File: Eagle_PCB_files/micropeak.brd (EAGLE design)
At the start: 100 x 80 mm, 15 parts, among them U1 ATTINY85-20MUR, U2 MS5611-01BA03

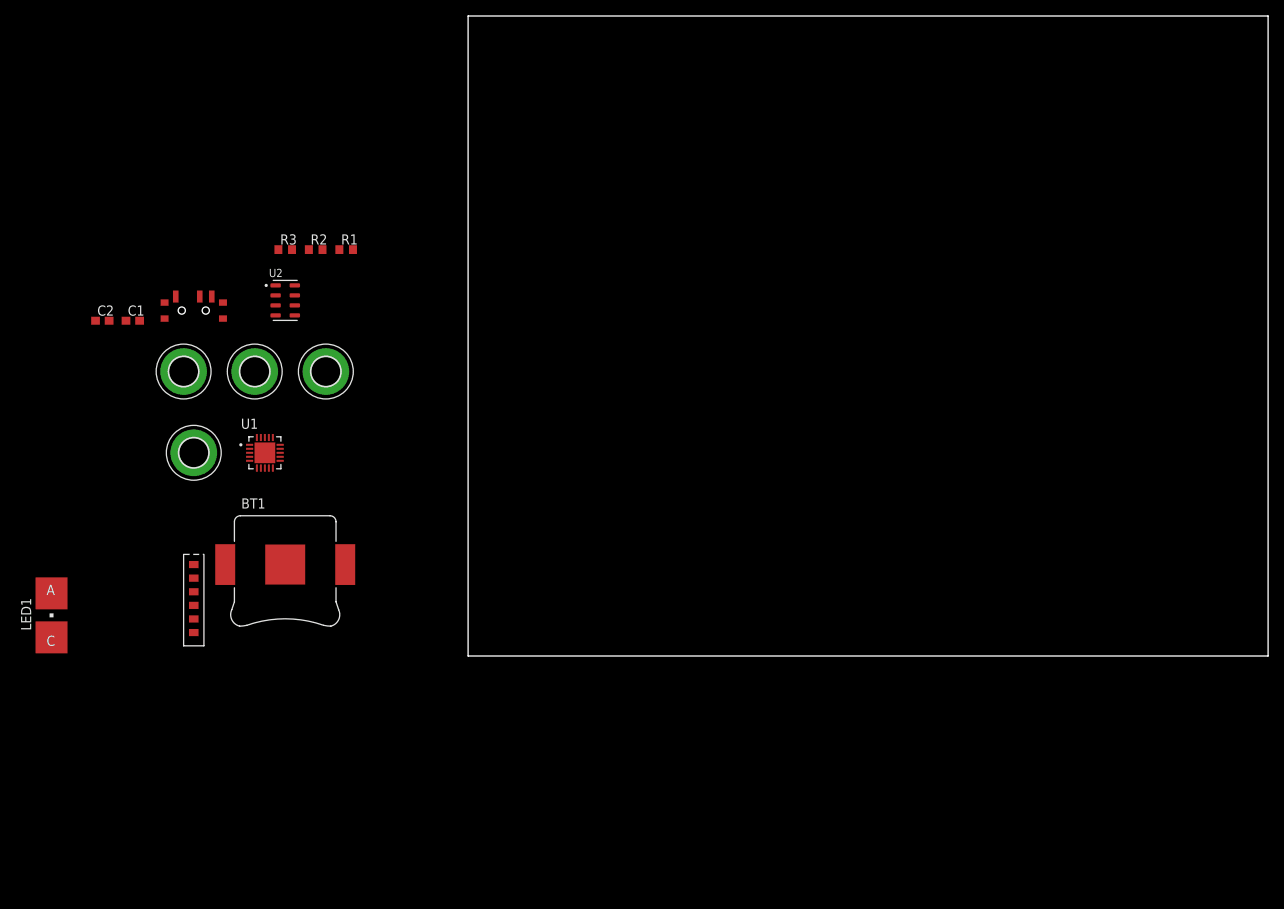
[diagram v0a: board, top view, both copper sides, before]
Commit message: replaced mounting holes with correct size hole
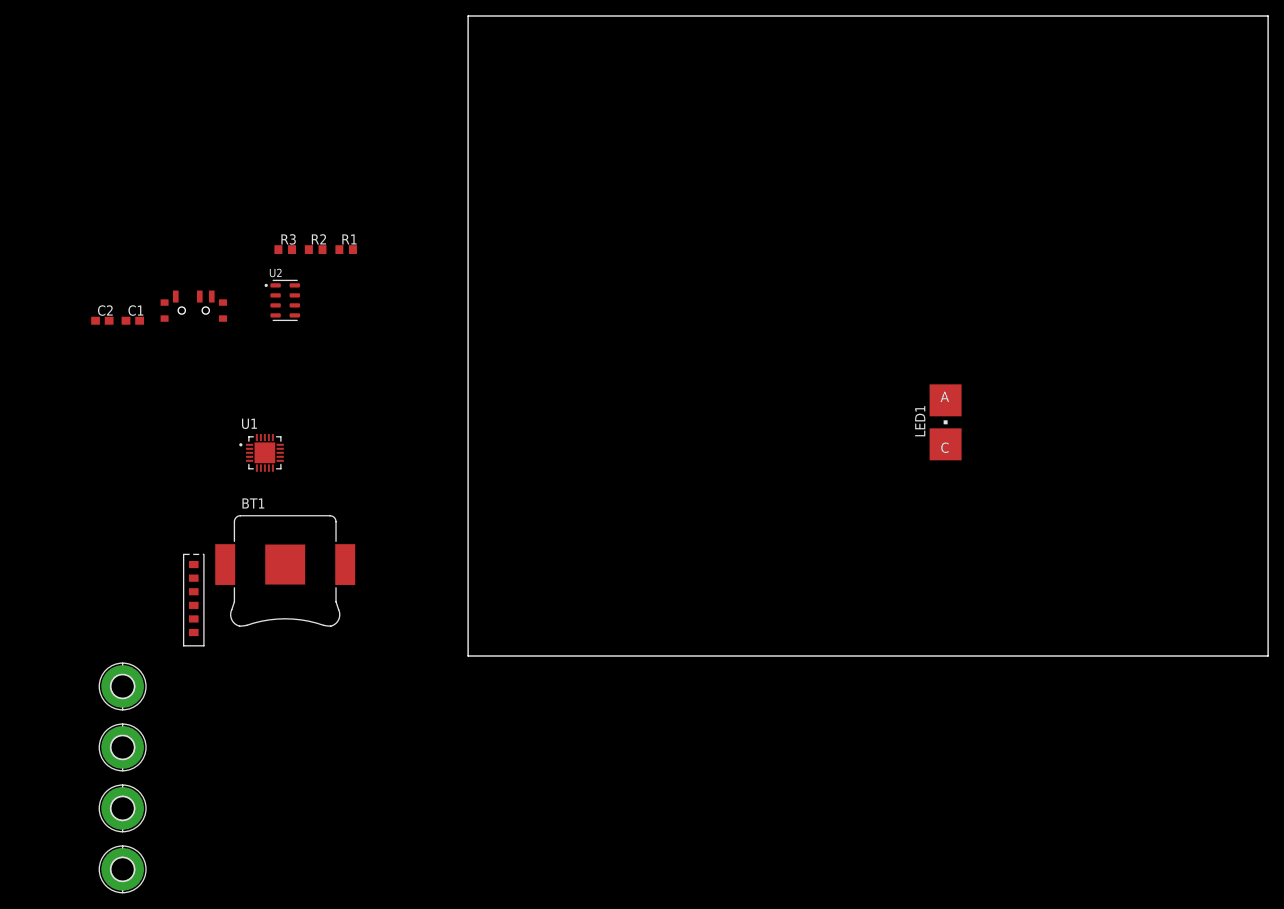
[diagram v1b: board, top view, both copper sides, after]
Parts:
- removed H5: MOUNT-PAD-ROUND3.6, holes:3,6-PAD
- added H4: MOUNT-PAD-ROUND2.8, holes:2,8-PAD
- H1, H2, H3: value MOUNT-PAD-ROUND3.6 -> MOUNT-PAD-ROUND2.8; device holes:3,6-PAD -> holes:2,8-PAD
- moved LED1 114.3 mm to (59.7, 29.2)
- moved H3 64.4 mm to (-43.2, -26.7)
- moved H2 60.2 mm to (-43.2, -19.1)
- moved H1 37.9 mm to (-43.2, -11.4)
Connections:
- net +3V3: now also H1.B2,8, H2.B2,8, H3.B2,8, H4.B2,8; no longer H1.B3,6, H2.B3,6, H3.B3,6, H5.B3,6
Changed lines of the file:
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@@
 <attribute name="VALUE" x="-46.355" y="40.005" size="1.27" layer="27"/>
-</element>
-<element name="H1" library="holes" library_urn="urn:adsk.eagle:library:237" package="3,6-PAD" package3d_urn="urn:adsk.eagle:package:14284/1" value="MOUNT-PAD-ROUND3.6" x="-34.29" y="25.4" smashed="yes">
-<attribute name="POPULARITY" value="0" x="0" y="0" size="1.778" layer="27" display="off"/>
-</element>
-<element name="H2" library="holes" library_urn="urn:adsk.eagle:library:237" package="3,6-PAD" package3d_urn="urn:adsk.eagle:package:14284/1" value="MOUNT-PAD-ROUND3.6" x="-17.78" y="35.56" smashed="yes">
-<attribute name="POPULARITY" value="0" x="0" y="0" size="1.778" layer="27" display="off"/>
-</element>
-<element name="H3" library="holes" library_urn="urn:adsk.eagle:library:237" package="3,6-PAD" package3d_urn="urn:adsk.eagle:package:14284/1" value="MOUNT-PAD-ROUND3.6" x="-26.67" y="35.56" smashed="yes">
-<attribute name="POPULARITY" value="0" x="0" y="0" size="1.778" layer="27" display="off"/>
-</element>
-<element name="H5" library="holes" library_urn="urn:adsk.eagle:library:237" package="3,6-PAD" package3d_urn="urn:adsk.eagle:package:14284/1" value="MOUNT-PAD-ROUND3.6" x="-35.56" y="35.56" smashed="yes">
-<attribute name="POPULARITY" value="0" x="0" y="0" size="1.778" layer="27" display="off"/>
 </element>
 <element name="R1" library="rcl" library_urn="urn:adsk.eagle:library:334" package="R0603" package3d_urn="urn:adsk.eagle:package:23555/3" value="" x="-15.24" y="50.8" smashed="yes">
@@
 <attribute name="VALUE" x="-24.995009375" y="40.68493125" size="1.016" layer="27"/>
 </element>
-<element name="LED1" library="led" library_urn="urn:adsk.eagle:library:259" package="P-LCC-2" package3d_urn="urn:adsk.eagle:package:15817/1" value="" x="-52.07" y="5.08" smashed="yes">
-<attribute name="NAME" x="-54.61" y="3.175" size="1.27" layer="25" rot="R90"/>
-<attribute name="POPULARITY" value="2" x="-52.07" y="5.08" size="1.778" layer="27" display="off"/>
-<attribute name="VALUE" x="-48.26" y="3.175" size="1.27" layer="27" rot="R90"/>
+<element name="LED1" library="led" library_urn="urn:adsk.eagle:library:259" package="P-LCC-2" package3d_urn="urn:adsk.eagle:package:15817/1" value="" x="59.69" y="29.21" smashed="yes">
+<attribute name="NAME" x="57.15" y="27.305" size="1.27" layer="25" rot="R90"/>
+<attribute name="POPULARITY" value="2" x="59.69" y="29.21" size="1.778" layer="27" display="off"/>
+<attribute name="VALUE" x="63.5" y="27.305" size="1.27" layer="27" rot="R90"/>
+</element>
+<element name="H4" library="holes" library_urn="urn:adsk.eagle:library:237" package="2,8-PAD" package3d_urn="urn:adsk.eagle:package:14281/1" value="MOUNT-PAD-ROUND2.8" x="-43.18" y="-3.81" smashed="yes">
+<attribute name="POPULARITY" value="6" x="-43.18" y="-3.81" size="1.778" layer="27" display="off"/>
+</element>
+<element name="H1" library="holes" library_urn="urn:adsk.eagle:library:237" package="2,8-PAD" package3d_urn="urn:adsk.eagle:package:14281/1" value="MOUNT-PAD-ROUND2.8" x="-43.18" y="-11.43" smashed="yes">
+<attribute name="POPULARITY" value="6" x="-43.18" y="-11.43" size="1.778" layer="27" display="off"/>
+</element>
+<element name="H2" library="holes" library_urn="urn:adsk.eagle:library:237" package="2,8-PAD" package3d_urn="urn:adsk.eagle:package:14281/1" value="MOUNT-PAD-ROUND2.8" x="-43.18" y="-19.05" smashed="yes">
+<attribute name="POPULARITY" value="6" x="-43.18" y="-19.05" size="1.778" layer="27" display="off"/>
+</element>
+<element name="H3" library="holes" library_urn="urn:adsk.eagle:library:237" package="2,8-PAD" package3d_urn="urn:adsk.eagle:package:14281/1" value="MOUNT-PAD-ROUND2.8" x="-43.18" y="-26.67" smashed="yes">
+<attribute name="POPULARITY" value="6" x="-43.18" y="-26.67" size="1.778" layer="27" display="off"/>
 </element>
 </elements>
@@
 <contactref element="U$2" pad="P$6"/>
 <contactref element="LED1" pad="C"/>
-<wire x1="-34.29" y1="2.93" x2="-52.07" y2="2.33" width="0" layer="19" extent="1-1"/>
+<wire x1="-34.29" y1="2.93" x2="59.69" y2="26.46" width="0" layer="19" extent="1-1"/>
 <wire x1="-25.4" y1="23.49" x2="-34.29" y2="2.93" width="0" layer="19" extent="1-1"/>
 <wire x1="-25.4" y1="25.4" x2="-25.4" y2="23.49" width="0" layer="19" extent="1-1"/>
@@
 <contactref element="C2" pad="1"/>
 <contactref element="U$2" pad="P$2"/>
-<contactref element="H5" pad="B3,6"/>
-<contactref element="H1" pad="B3,6"/>
-<contactref element="H2" pad="B3,6"/>
-<contactref element="H3" pad="B3,6"/>
-<wire x1="-24.06" y1="46.325" x2="-18.2" y2="50.8" width="0" layer="19" extent="1-1"/>
-<wire x1="-26.67" y1="35.56" x2="-24.06" y2="46.325" width="0" layer="19" extent="1-1"/>
-<wire x1="-17.78" y1="35.56" x2="-26.67" y2="35.56" width="0" layer="19" extent="1-1"/>
-<wire x1="-35.56" y1="35.56" x2="-26.67" y2="35.56" width="0" layer="19" extent="1-1"/>
-<wire x1="-42.76" y1="41.91" x2="-35.56" y2="35.56" width="0" layer="19" extent="1-1"/>
+<contactref element="H4" pad="B2,8"/>
+<contactref element="H1" pad="B2,8"/>
+<contactref element="H2" pad="B2,8"/>
+<contactref element="H3" pad="B2,8"/>
+<wire x1="-43.18" y1="-19.05" x2="-43.18" y2="-26.67" width="0" layer="19" extent="1-1"/>
+<wire x1="-43.18" y1="-11.43" x2="-43.18" y2="-19.05" width="0" layer="19" extent="1-1"/>
+<wire x1="-43.18" y1="-3.81" x2="-43.18" y2="-11.43" width="0" layer="19" extent="1-1"/>
+<wire x1="-34.29" y1="9.73" x2="-43.18" y2="-3.81" width="0" layer="19" extent="1-1"/>
+<wire x1="-30.36" y1="11.43" x2="-34.29" y2="9.73" width="0" layer="19" extent="1-1"/>
+<wire x1="-15.36" y1="11.43" x2="-30.36" y2="11.43" width="0" layer="19" extent="1-1"/>
+<wire x1="-23.49" y1="26.4" x2="-30.36" y2="11.43" width="0" layer="19" extent="1-1"/>
+<wire x1="-24.06" y1="46.325" x2="-23.49" y2="26.4" width="0" layer="19" extent="1-1"/>
+<wire x1="-18.2" y1="50.8" x2="-24.06" y2="46.325" width="0" layer="19" extent="1-1"/>
+<wire x1="-42.76" y1="41.91" x2="-24.06" y2="46.325" width="0" layer="19" extent="1-1"/>
 <wire x1="-46.57" y1="41.91" x2="-42.76" y2="41.91" width="0" layer="19" extent="1-1"/>
-<wire x1="-23.49" y1="26.4" x2="-26.67" y2="35.56" width="0" layer="19" extent="1-1"/>
-<wire x1="-34.29" y1="25.4" x2="-35.56" y2="35.56" width="0" layer="19" extent="1-1"/>
-<wire x1="-30.36" y1="11.43" x2="-34.29" y2="25.4" width="0" layer="19" extent="1-1"/>
-<wire x1="-34.29" y1="9.73" x2="-30.36" y2="11.43" width="0" layer="19" extent="1-1"/>
-<wire x1="-15.36" y1="11.43" x2="-30.36" y2="11.43" width="0" layer="19" extent="1-1"/>
 </signal>
 <signal name="N$3">
@@
 <contactref element="LED1" pad="A"/>
 <contactref element="R1" pad="2"/>
-<wire x1="-14.39" y1="50.8" x2="-52.07" y2="7.83" width="0" layer="19" extent="1-1"/>
+<wire x1="-14.39" y1="50.8" x2="59.69" y2="31.96" width="0" layer="19" extent="1-1"/>
 </signal>
 </signals>
